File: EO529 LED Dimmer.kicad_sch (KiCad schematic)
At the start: 35 parts, among them J1 VBat, Q1 BC639, Q2 BC639, Q3 BC639, Q4 BC639, U1 LM339, U2 NE555P

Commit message: Revert "New layout, less parts"
This reverts commit 43836197f3911cfe2976812753205c060315a555.
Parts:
- removed U1: LM339, Package_DIP:DIP-14_W7.62mm_Socket, symbol Comparator:LM339
- removed U2: NE555P, Package_DIP:DIP-8_W7.62mm_Socket, symbol Timer:NE555P
- added C3, C4, C5, C6, C7, C8: 10n, Capacitor_THT:C_Disc_D5.0mm_W2.5mm_P5.00mm, symbol Device:C_Small
- added R13, R14, R19, R20, R7, R8: 10k, Resistor_THT:R_Axial_DIN0207_L6.3mm_D2.5mm_P7.62mm_Horizontal, symbol Device:R_Small
- added TP1, TP2: TestPoint, TestPoint:TestPoint_THTPad_D2.0mm_Drill1.0mm, symbol Connector:TestPoint
- added U1, U2: NE556, Package_DIP:DIP-14_W7.62mm_Socket, symbol Timer:NE556
- added U3, U4: LM393, Package_DIP:DIP-8_W7.62mm_Socket, symbol Comparator:LM393
- C9: renamed from C3; value 100u -> 10u; footprint Capacitor_THT:CP_Radial_D8.0mm_P3.50mm -> Capacitor_THT:CP_Radial_D5.0mm_P2.50mm
- Q1, Q4: footprint Package_TO_SOT_THT:TO-92_Inline_Wide -> Package_TO_SOT_THT:TO-92
- Q2: renamed from Q3; footprint Package_TO_SOT_THT:TO-92_Inline_Wide -> Package_TO_SOT_THT:TO-92
- Q3: renamed from Q2; footprint Package_TO_SOT_THT:TO-92_Inline_Wide -> Package_TO_SOT_THT:TO-92
- R12: renamed from R17; footprint Resistor_THT:R_Axial_DIN0207_L6.3mm_D2.5mm_P7.62mm_Horizontal -> Resistor_THT:R_Axial_DIN0414_L11.9mm_D4.5mm_P15.24mm_Horizontal
- R18: renamed from R10; footprint Resistor_THT:R_Axial_DIN0207_L6.3mm_D2.5mm_P7.62mm_Horizontal -> Resistor_THT:R_Axial_DIN0414_L11.9mm_D4.5mm_P15.24mm_Horizontal
- R24: renamed from R18; footprint Resistor_THT:R_Axial_DIN0207_L6.3mm_D2.5mm_P7.62mm_Horizontal -> Resistor_THT:R_Axial_DIN0414_L11.9mm_D4.5mm_P15.24mm_Horizontal
- R6: renamed from R9; footprint Resistor_THT:R_Axial_DIN0207_L6.3mm_D2.5mm_P7.62mm_Horizontal -> Resistor_THT:R_Axial_DIN0414_L11.9mm_D4.5mm_P15.24mm_Horizontal
- renumbered C4 to C10, D2 to D1, D1 to D2, R12 to R10, R15 to R11, R5 to R15, R6 to R16, R8 to R17, R13 to R21, R14 to R22, R16 to R23, R7 to R5, R11 to R9, RV3 to RV2, RV2 to RV3
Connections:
- net GND: now also C3.2, C4.2, C5.2, C6.2, C7.2, C8.2, U1.7 (GND), U1.7 (GND), U2.7 (GND), U2.7 (GND), U3.4 (V-), U4.4 (V-)
- net VCC: now also R13.1, R19.1, R7.1, TP2.1, U1.10 (R), U1.14 (VCC), U1.14 (VCC), U1.4 (R), U2.10 (R), U2.14 (VCC), U2.14 (VCC), U2.4 (R), U3.8 (V+), U4.8 (V+); no longer D1.2 (A), D2.4 (A)
- net at RV1.2: now also U3.6 (_)
- net at C1.1: now also U1.3 (CV)
- net at R1.2, R2.1: now also U1.1 (DIS)
- net at Q1.3 (B), R5.1: now also U3.7
- net at RV2.1: now also R10.1; no longer R9.2
- net at RV2.2: now also U4.2 (-)
- net at RV2.3: now also R9.2; no longer R10.1
- net at Q2.3 (B), R11.1: now also U4.1
- net at RV3.2: now also U4.6 (_)
- net at Q3.3 (B), R17.1: now also U4.7
- net at RV4.1: now also R22.1; no longer R21.2
- net at RV4.2: now also U3.2 (-)
- net at RV4.3: now also R21.2; no longer R22.1
- net at Q4.3 (B), R23.1: now also U3.1
- net PWM: no longer names the net of C2.1, R2.2
- net PWM: now also U1.2 (THR), U1.6 (TR), U3.5 (+)
- new net: C3.1, U1.11 (CV)
- new net: C4.1, R8.2, U1.12 (THR), U1.8 (TR), U4.3 (+)
- new net: R7.2, R8.1, U1.13 (DIS)
- new net: C6.1, R14.2, U2.2 (THR), U2.6 (TR), U4.5 (+)
- new net: R13.2, R14.1, U2.1 (DIS)
- new net: C5.1, U2.3 (CV)
- new net: C7.1, U2.11 (CV)
- new net: C8.1, R20.2, U2.12 (THR), U2.8 (TR), U3.3 (+)
- new net: R19.2, R20.1, U2.13 (DIS)
- new net V_LED: D1.2 (A), D2.4 (A), TP1.1
- no-connect marks 1 -> 4
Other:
- moved on the sheet: C1, C10, C2, C9, D1, D2, J1, Q1, Q2, Q3, Q4, R1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

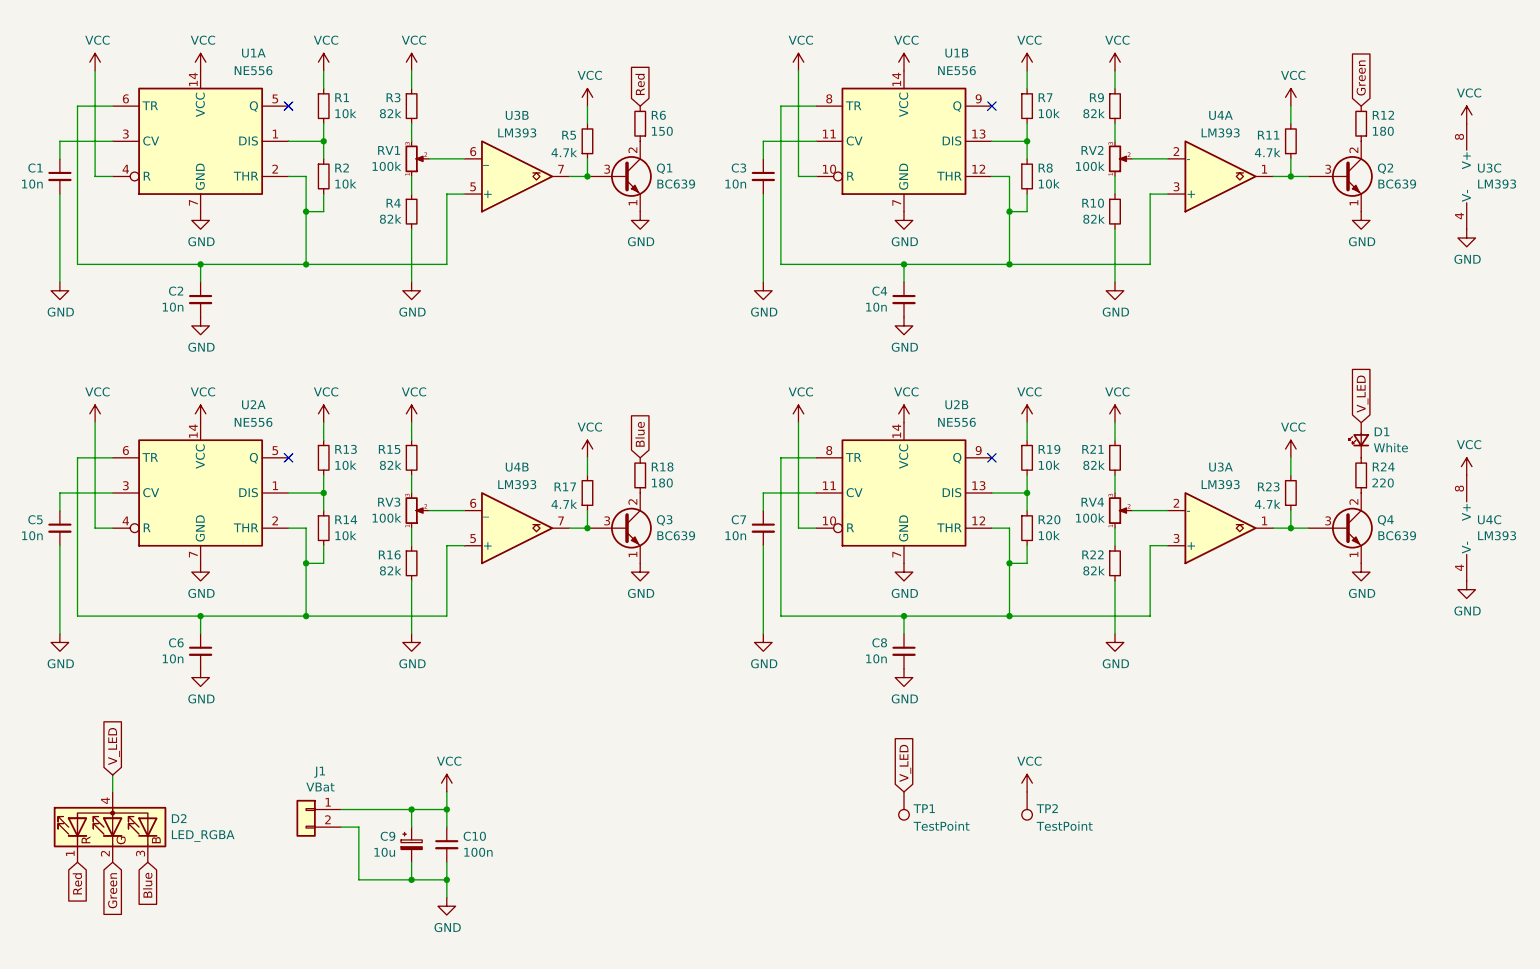
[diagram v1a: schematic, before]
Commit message: New layout, less parts
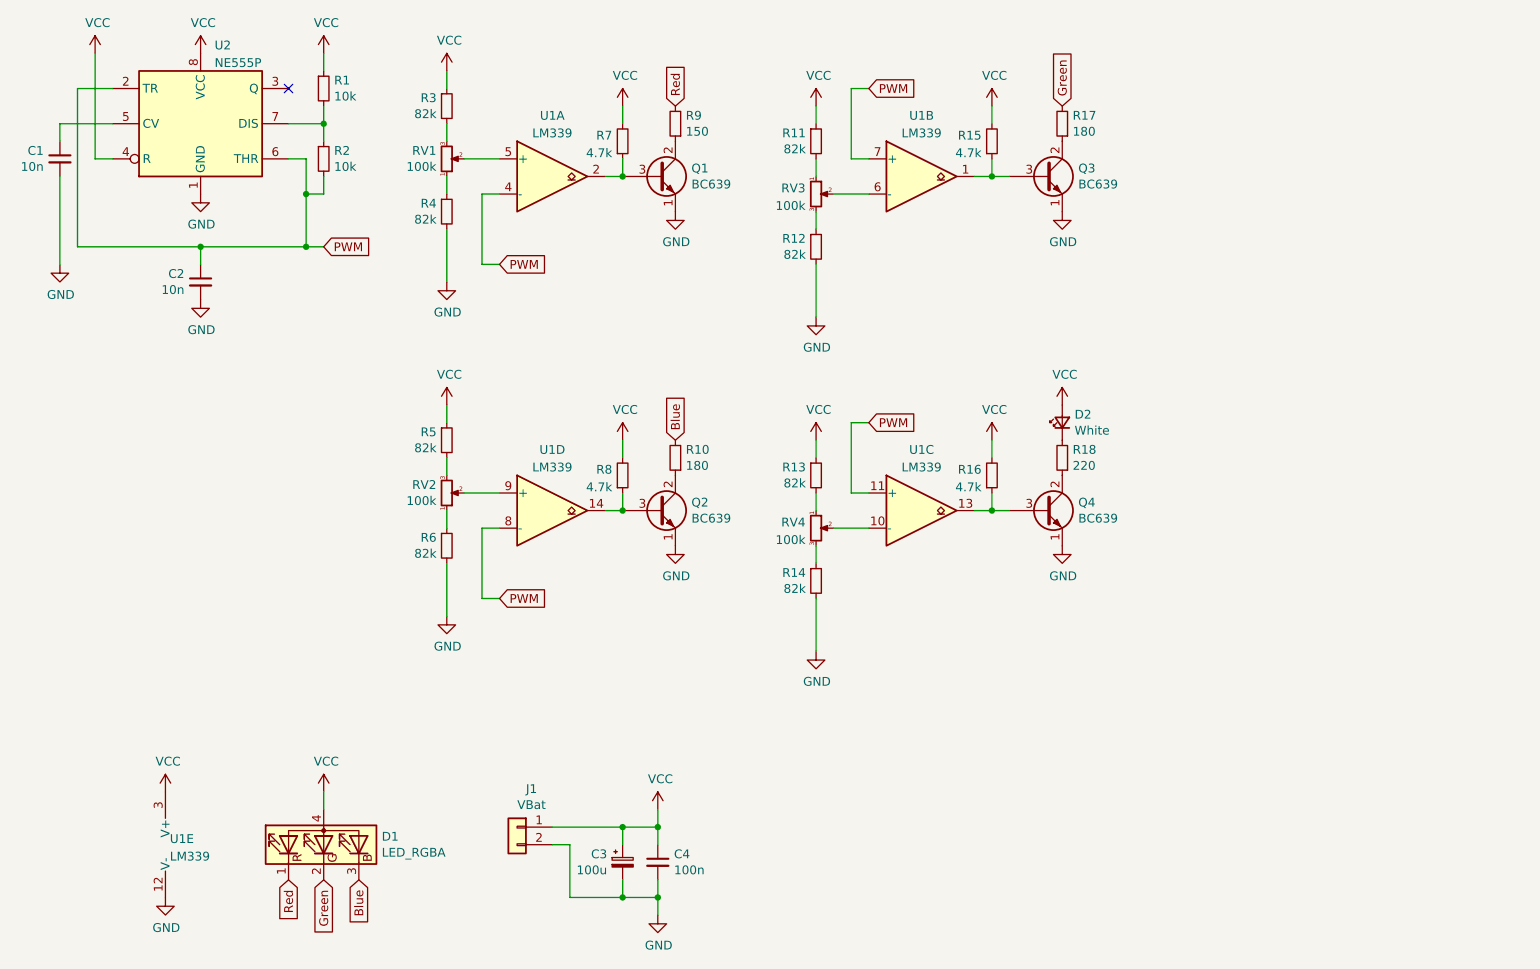
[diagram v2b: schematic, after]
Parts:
- removed C3, C4, C5, C6, C7, C8: 10n, Capacitor_THT:C_Disc_D5.0mm_W2.5mm_P5.00mm, symbol Device:C_Small
- removed R13, R14, R19, R20, R7, R8: 10k, Resistor_THT:R_Axial_DIN0207_L6.3mm_D2.5mm_P7.62mm_Horizontal, symbol Device:R_Small
- removed TP1, TP2: TestPoint, TestPoint:TestPoint_THTPad_D2.0mm_Drill1.0mm, symbol Connector:TestPoint
- removed U1, U2: NE556, Package_DIP:DIP-14_W7.62mm_Socket, symbol Timer:NE556
- removed U3, U4: LM393, Package_DIP:DIP-8_W7.62mm_Socket, symbol Comparator:LM393
- added U1: LM339, Package_DIP:DIP-14_W7.62mm_Socket, symbol Comparator:LM339
- added U2: NE555P, Package_DIP:DIP-8_W7.62mm_Socket, symbol Timer:NE555P
- C3: renamed from C9; value 10u -> 100u; footprint Capacitor_THT:CP_Radial_D5.0mm_P2.50mm -> Capacitor_THT:CP_Radial_D8.0mm_P3.50mm
- Q1, Q4: footprint Package_TO_SOT_THT:TO-92 -> Package_TO_SOT_THT:TO-92_Inline_Wide
- Q2: renamed from Q3; footprint Package_TO_SOT_THT:TO-92 -> Package_TO_SOT_THT:TO-92_Inline_Wide
- Q3: renamed from Q2; footprint Package_TO_SOT_THT:TO-92 -> Package_TO_SOT_THT:TO-92_Inline_Wide
- R10: renamed from R18; footprint Resistor_THT:R_Axial_DIN0414_L11.9mm_D4.5mm_P15.24mm_Horizontal -> Resistor_THT:R_Axial_DIN0207_L6.3mm_D2.5mm_P7.62mm_Horizontal
- R17: renamed from R12; footprint Resistor_THT:R_Axial_DIN0414_L11.9mm_D4.5mm_P15.24mm_Horizontal -> Resistor_THT:R_Axial_DIN0207_L6.3mm_D2.5mm_P7.62mm_Horizontal
- R18: renamed from R24; footprint Resistor_THT:R_Axial_DIN0414_L11.9mm_D4.5mm_P15.24mm_Horizontal -> Resistor_THT:R_Axial_DIN0207_L6.3mm_D2.5mm_P7.62mm_Horizontal
- R9: renamed from R6; footprint Resistor_THT:R_Axial_DIN0414_L11.9mm_D4.5mm_P15.24mm_Horizontal -> Resistor_THT:R_Axial_DIN0207_L6.3mm_D2.5mm_P7.62mm_Horizontal
- renumbered C10 to C4, D2 to D1, D1 to D2, R9 to R11, R10 to R12, R21 to R13, R22 to R14, R11 to R15, R23 to R16, R15 to R5, R16 to R6, R5 to R7, R17 to R8, RV3 to RV2, RV2 to RV3
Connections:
- net V_LED is gone; now on net VCC: D1.4 (A), D2.2 (A)
- net GND: now also U1.12 (V-), U2.1 (GND)
- net VCC: now also U1.3 (V+), U2.4 (R), U2.8 (VCC)
- net at R1.2, R2.1: now also U2.7 (DIS)
- net PWM: now reaches C2.1, R2.2
- net PWM: now also U1.11 (+), U1.4 (-), U1.7 (+), U1.8 (-), U2.2 (TR), U2.6 (THR)
- net at C1.1: now also U2.5 (CV)
- net at RV1.2: now also U1.5 (+)
- net at Q1.3 (B), R7.1: now also U1.2
- net at RV3.1: now also R11.2; no longer R12.1
- net at RV3.2: now also U1.6 (-)
- net at RV3.3: now also R12.1; no longer R11.2
- net at Q3.3 (B), R15.1: now also U1.1
- net at RV2.2: now also U1.9 (+)
- net at Q2.3 (B), R8.1: now also U1.14
- net at RV4.1: now also R13.2; no longer R14.1
- net at RV4.2: now also U1.10 (-)
- net at RV4.3: now also R14.1; no longer R13.2
- net at Q4.3 (B), R16.1: now also U1.13
- no-connect marks 4 -> 1
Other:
- moved on the sheet: C1, C2, C3, C4, D1, D2, J1, Q1, Q2, Q3, Q4, R1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
